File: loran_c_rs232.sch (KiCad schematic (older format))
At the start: 30 parts, among them P301 UART1 3V3, P302 DB9 Ribbon 1, P303 DB9 Ribbon 2, U301 ST3232, U302 ST3232, U303 ST3232

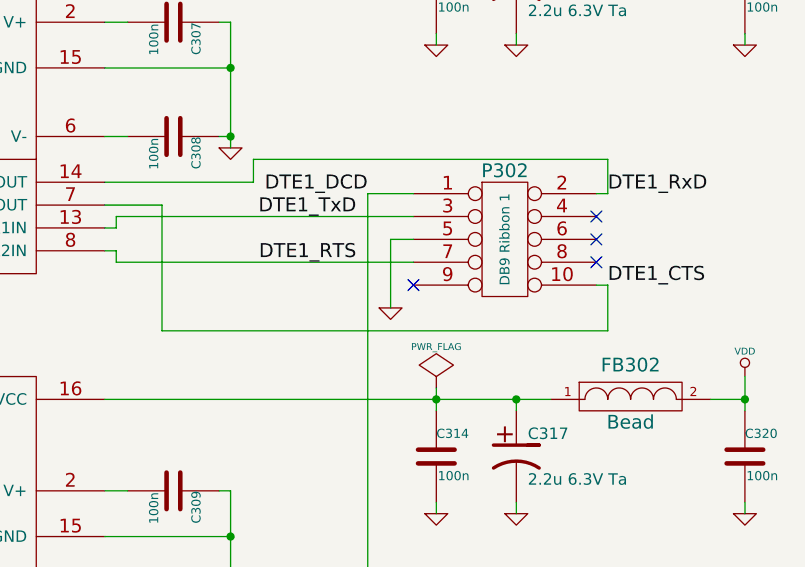
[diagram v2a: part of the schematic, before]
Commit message: Update: fix, assign modules to components -Fix P302 incorrect connection -Assign footprints to components (not all yet) -Back-import footprints into schematic fields
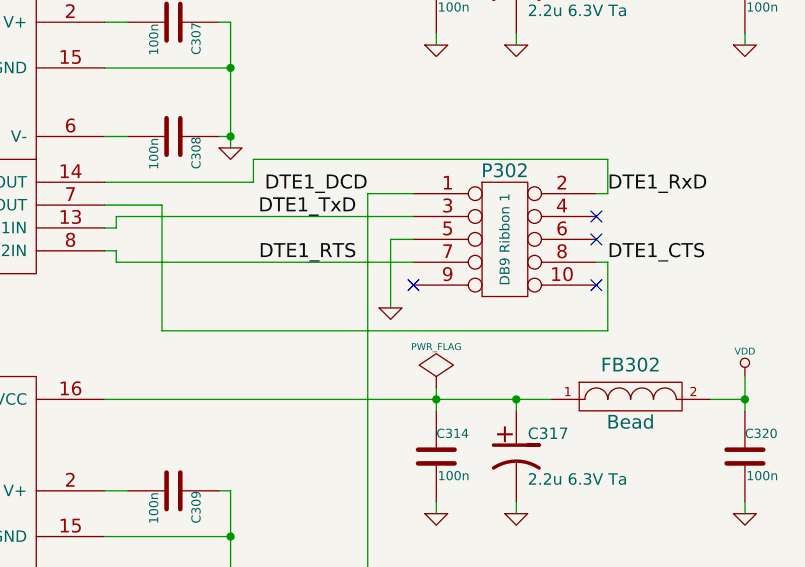
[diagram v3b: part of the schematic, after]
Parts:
- C301, C302, C303, C304, C305, C306, C307, C308, C309, C310, C311, C312, C313, C314, C315, C319, C320, C321: footprint (none) -> w_smd_capacitors:c_1206
- C316, C317, C318: footprint (none) -> w_smd_capacitors:c_tant_A
- FB301, FB302, FB303: footprint (none) -> w_pth_resistors:RC07
- P301: footprint (none) -> Pin_Headers:Pin_Header_Straight_1x06
- P302, P303: footprint (none) -> w_conn_strip:vasch_strip_5x2
- U301, U302, U303: footprint (none) -> w_smd_dil:so-16
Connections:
- net DTE1_CTS: now also P302.8; no longer P302.10
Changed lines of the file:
@@
 Date "18 янв. 2014"
 Rev ""
-Comp "Roman Dobrodiy"
+Comp "Roman Dobrodiy (aka RomaVis)"
 Comment1 ""
 Comment2 ""
@@
 F 0 "U301" H 3550 3550 70  0000 C CNN
 F 1 "ST3232" H 3550 1850 70  0000 C CNN
-F 2 "" H 3550 2700 60  0000 C CNN
+F 2 "w_smd_dil:so-16" H 3550 2700 60  0001 C CNN
 F 3 "" H 3550 2700 60  0000 C CNN
 	1    3550 2700
@@
 F 0 "P303" H 6100 7750 60  0000 C CNN
 F 1 "DB9 Ribbon 2" V 6100 7450 43  0000 C CNN
-F 2 "" H 6100 7450 60  0000 C CNN
+F 2 "w_conn_strip:vasch_strip_5x2" H 6100 7450 60  0001 C CNN
 F 3 "" H 6100 7450 60  0000 C CNN
 	1    6100 7450
@@
 F 0 "P302" H 6100 3650 60  0000 C CNN
 F 1 "DB9 Ribbon 1" V 6100 3350 43  0000 C CNN
-F 2 "" H 6100 3350 60  0000 C CNN
+F 2 "w_conn_strip:vasch_strip_5x2" H 6100 3350 60  0001 C CNN
 F 3 "" H 6100 3350 60  0000 C CNN
 	1    6100 3350
@@
 Text Label 6550 3150 0    61   ~ 0
 DTE1_RxD
-Text Label 6550 3550 0    61   ~ 0
+Text Label 6550 3450 0    61   ~ 0
 DTE1_CTS
 $Comp
@@
 F 0 "C308" H 4650 3000 40  0000 L CNN
 F 1 "100n" H 4656 2815 40  0000 L CNN
-F 2 "" H 4688 2750 30  0000 C CNN
+F 2 "w_smd_capacitors:c_1206" H 4688 2750 30  0001 C CNN
 F 3 "" H 4650 2900 60  0000 C CNN
 	1    4650 2900
@@
 F 0 "C307" H 4650 2500 40  0000 L CNN
 F 1 "100n" H 4656 2315 40  0000 L CNN
-F 2 "" H 4688 2250 30  0000 C CNN
+F 2 "w_smd_capacitors:c_1206" H 4688 2250 30  0001 C CNN
 F 3 "" H 4650 2400 60  0000 C CNN
 	1    4650 2400
@@
 F 0 "C301" H 2450 2300 40  0000 L CNN
 F 1 "100n" H 2456 2115 40  0000 L CNN
-F 2 "" H 2488 2050 30  0000 C CNN
+F 2 "w_smd_capacitors:c_1206" H 2488 2050 30  0001 C CNN
 F 3 "" H 2450 2200 60  0000 C CNN
 	1    2450 2200
@@
 F 0 "C302" H 2450 2800 40  0000 L CNN
 F 1 "100n" H 2456 2615 40  0000 L CNN
-F 2 "" H 2488 2550 30  0000 C CNN
+F 2 "w_smd_capacitors:c_1206" H 2488 2550 30  0001 C CNN
 F 3 "" H 2450 2700 60  0000 C CNN
 	1    2450 2700
@@
 	4600 3200 4600 3750
 Wire Wire Line
-	4600 3750 6550 3750
-Wire Wire Line
-	6550 3750 6550 3550
-Wire Wire Line
-	6550 3550 6500 3550
+	6550 3750 4600 3750
+Wire Wire Line
+	6550 3450 6550 3750
 $Comp
 L MAX232 U303
@@
 F 0 "U303" H 3550 7650 70  0000 C CNN
 F 1 "ST3232" H 3550 5950 70  0000 C CNN
-F 2 "" H 3550 6800 60  0000 C CNN
+F 2 "w_smd_dil:so-16" H 3550 6800 60  0001 C CNN
 F 3 "" H 3550 6800 60  0000 C CNN
 	1    3550 6800
@@
 F 0 "C312" H 4650 7100 40  0000 L CNN
 F 1 "100n" H 4656 6915 40  0000 L CNN
-F 2 "" H 4688 6850 30  0000 C CNN
+F 2 "w_smd_capacitors:c_1206" H 4688 6850 30  0001 C CNN
 F 3 "" H 4650 7000 60  0000 C CNN
 	1    4650 7000
@@
 F 0 "C311" H 4650 6600 40  0000 L CNN
 F 1 "100n" H 4656 6415 40  0000 L CNN
-F 2 "" H 4688 6350 30  0000 C CNN
+F 2 "w_smd_capacitors:c_1206" H 4688 6350 30  0001 C CNN
 F 3 "" H 4650 6500 60  0000 C CNN
 	1    4650 6500
@@
 F 0 "C303" H 2450 6400 40  0000 L CNN
 F 1 "100n" H 2456 6215 40  0000 L CNN
-F 2 "" H 2488 6150 30  0000 C CNN
+F 2 "w_smd_capacitors:c_1206" H 2488 6150 30  0001 C CNN
 F 3 "" H 2450 6300 60  0000 C CNN
 	1    2450 6300
@@
 F 0 "C304" H 2450 6900 40  0000 L CNN
 F 1 "100n" H 2456 6715 40  0000 L CNN
-F 2 "" H 2488 6650 30  0000 C CNN
+F 2 "w_smd_capacitors:c_1206" H 2488 6650 30  0001 C CNN
 F 3 "" H 2450 6800 60  0000 C CNN
 	1    2450 6800
@@
 F 0 "U302" H 3550 5600 70  0000 C CNN
 F 1 "ST3232" H 3550 3900 70  0000 C CNN
-F 2 "" H 3550 4750 60  0000 C CNN
+F 2 "w_smd_dil:so-16" H 3550 4750 60  0001 C CNN
 F 3 "" H 3550 4750 60  0000 C CNN
 	1    3550 4750
@@
 F 0 "C310" H 4650 5050 40  0000 L CNN
 F 1 "100n" H 4656 4865 40  0000 L CNN
-F 2 "" H 4688 4800 30  0000 C CNN
+F 2 "w_smd_capacitors:c_1206" H 4688 4800 30  0001 C CNN
 F 3 "" H 4650 4950 60  0000 C CNN
 	1    4650 4950
@@
 F 0 "C309" H 4650 4550 40  0000 L CNN
 F 1 "100n" H 4656 4365 40  0000 L CNN
-F 2 "" H 4688 4300 30  0000 C CNN
+F 2 "w_smd_capacitors:c_1206" H 4688 4300 30  0001 C CNN
 F 3 "" H 4650 4450 60  0000 C CNN
 	1    4650 4450
@@
 F 0 "C305" H 2600 4350 40  0000 L CNN
 F 1 "100n" H 2606 4165 40  0000 L CNN
-F 2 "" H 2638 4100 30  0000 C CNN
+F 2 "w_smd_capacitors:c_1206" H 2638 4100 30  0001 C CNN
 F 3 "" H 2600 4250 60  0000 C CNN
 	1    2600 4250
@@
 F 0 "C306" H 2600 4850 40  0000 L CNN
 F 1 "100n" H 2606 4665 40  0000 L CNN
-F 2 "" H 2638 4600 30  0000 C CNN
+F 2 "w_smd_capacitors:c_1206" H 2638 4600 30  0001 C CNN
 F 3 "" H 2600 4750 60  0000 C CNN
 	1    2600 4750
@@
 F 0 "C313" H 5800 2350 40  0000 L CNN
 F 1 "100n" H 5806 2165 40  0000 L CNN
-F 2 "" H 5838 2100 30  0000 C CNN
+F 2 "w_smd_capacitors:c_1206" H 5838 2100 30  0001 C CNN
 F 3 "" H 5800 2250 60  0000 C CNN
 	1    5800 2250
@@
 F 0 "C316" H 6200 2350 50  0000 L CNN
 F 1 "2.2u 6.3V Ta" H 6200 2150 50  0000 L CNN
-F 2 "" H 6150 2250 60  0000 C CNN
+F 2 "w_smd_capacitors:c_tant_A" H 6150 2250 60  0001 C CNN
 F 3 "" H 6150 2250 60  0000 C CNN
 	1    6150 2250
@@
 F 0 "FB301" H 6650 2150 60  0000 C CNN
 F 1 "Bead" H 6650 1900 60  0000 C CNN
-F 2 "" H 6650 2000 60  0000 C CNN
+F 2 "w_pth_resistors:RC07" H 6650 2000 60  0001 C CNN
 F 3 "" H 6650 2000 60  0000 C CNN
 	1    6650 2000
@@
 F 0 "C319" H 7150 2350 40  0000 L CNN
 F 1 "100n" H 7156 2165 40  0000 L CNN
-F 2 "" H 7188 2100 30  0000 C CNN
+F 2 "w_smd_capacitors:c_1206" H 7188 2100 30  0001 C CNN
 F 3 "" H 7150 2250 60  0000 C CNN
 	1    7150 2250
@@
 F 0 "C314" H 5800 4400 40  0000 L CNN
 F 1 "100n" H 5806 4215 40  0000 L CNN
-F 2 "" H 5838 4150 30  0000 C CNN
+F 2 "w_smd_capacitors:c_1206" H 5838 4150 30  0001 C CNN
 F 3 "" H 5800 4300 60  0000 C CNN
 	1    5800 4300
@@
 F 0 "C317" H 6200 4400 50  0000 L CNN
 F 1 "2.2u 6.3V Ta" H 6200 4200 50  0000 L CNN
-F 2 "" H 6150 4300 60  0000 C CNN
+F 2 "w_smd_capacitors:c_tant_A" H 6150 4300 60  0001 C CNN
 F 3 "" H 6150 4300 60  0000 C CNN
 	1    6150 4300
@@
 F 0 "FB302" H 6650 4200 60  0000 C CNN
 F 1 "Bead" H 6650 3950 60  0000 C CNN
-F 2 "" H 6650 4050 60  0000 C CNN
+F 2 "w_pth_resistors:RC07" H 6650 4050 60  0001 C CNN
 F 3 "" H 6650 4050 60  0000 C CNN
 	1    6650 4050
@@
 F 0 "C320" H 7150 4400 40  0000 L CNN
 F 1 "100n" H 7156 4215 40  0000 L CNN
-F 2 "" H 7188 4150 30  0000 C CNN
+F 2 "w_smd_capacitors:c_1206" H 7188 4150 30  0001 C CNN
 F 3 "" H 7150 4300 60  0000 C CNN
 	1    7150 4300
@@
 F 0 "C315" H 5800 6450 40  0000 L CNN
 F 1 "100n" H 5806 6265 40  0000 L CNN
-F 2 "" H 5838 6200 30  0000 C CNN
+F 2 "w_smd_capacitors:c_1206" H 5838 6200 30  0001 C CNN
 F 3 "" H 5800 6350 60  0000 C CNN
 	1    5800 6350
@@
 F 0 "C318" H 6200 6450 50  0000 L CNN
 F 1 "2.2u 6.3V Ta" H 6200 6250 50  0000 L CNN
-F 2 "" H 6150 6350 60  0000 C CNN
+F 2 "w_smd_capacitors:c_tant_A" H 6150 6350 60  0001 C CNN
 F 3 "" H 6150 6350 60  0000 C CNN
 	1    6150 6350
@@
 F 0 "FB303" H 6650 6250 60  0000 C CNN
 F 1 "Bead" H 6650 6000 60  0000 C CNN
-F 2 "" H 6650 6100 60  0000 C CNN
+F 2 "w_pth_resistors:RC07" H 6650 6100 60  0001 C CNN
 F 3 "" H 6650 6100 60  0000 C CNN
 	1    6650 6100
@@
 F 0 "C321" H 7150 6450 40  0000 L CNN
 F 1 "100n" H 7156 6265 40  0000 L CNN
-F 2 "" H 7188 6200 30  0000 C CNN
+F 2 "w_smd_capacitors:c_1206" H 7188 6200 30  0001 C CNN
 F 3 "" H 7150 6350 60  0000 C CNN
 	1    7150 6350
@@
 F 0 "P301" V 1550 4050 60  0000 C CNN
 F 1 "UART1 3V3" V 1650 4050 60  0000 C CNN
-F 2 "" H 1600 4050 60  0000 C CNN
+F 2 "Pin_Headers:Pin_Header_Straight_1x06" H 1600 4050 60  0001 C CNN
 F 3 "" H 1600 4050 60  0000 C CNN
 	1    1600 4050
@@
 NoConn ~ 6500 3250
 NoConn ~ 6500 3350
-NoConn ~ 6500 3450
 NoConn ~ 5700 3550
 Text HLabel 1200 3100 0    61   Input ~ 0
@@
 	1    0    0    -1
 $EndComp
+Wire Wire Line
+	6550 3450 6500 3450
+NoConn ~ 6500 3550
 $EndSCHEMATC
